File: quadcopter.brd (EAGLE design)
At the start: 130.1 x 130.1 mm, 76 parts, among them J1 AVR_SPI_PRG_6NS, J3 HEADER-0.1IN-2POS-FEMALE, J4 HEADER-0.1IN-2POS-FEMALE, J5 HEADER-0.1IN-2POS-FEMALE, J6 HEADER-0.1IN-2POS-FEMALE, SW1 PUSHBUTTON_SMD-VERTICAL, SW2 PUSHBUTTON_SMD-VERTICAL, U1 ATMEGA128RFA1

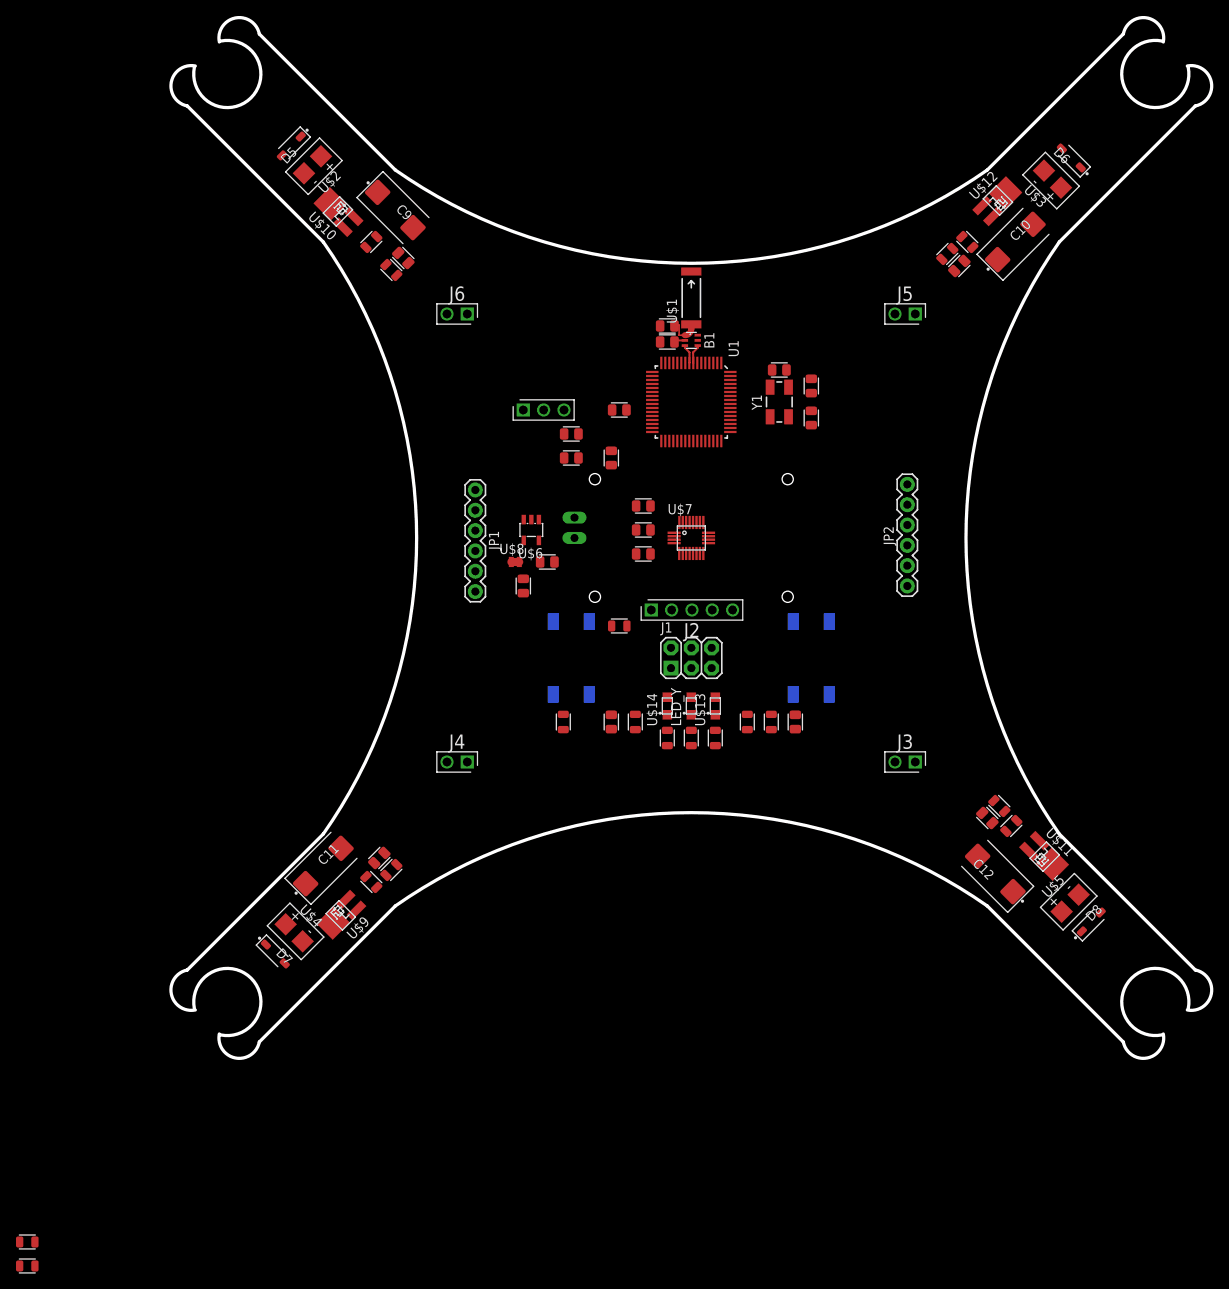
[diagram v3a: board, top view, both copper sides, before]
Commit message: layed down bat plane
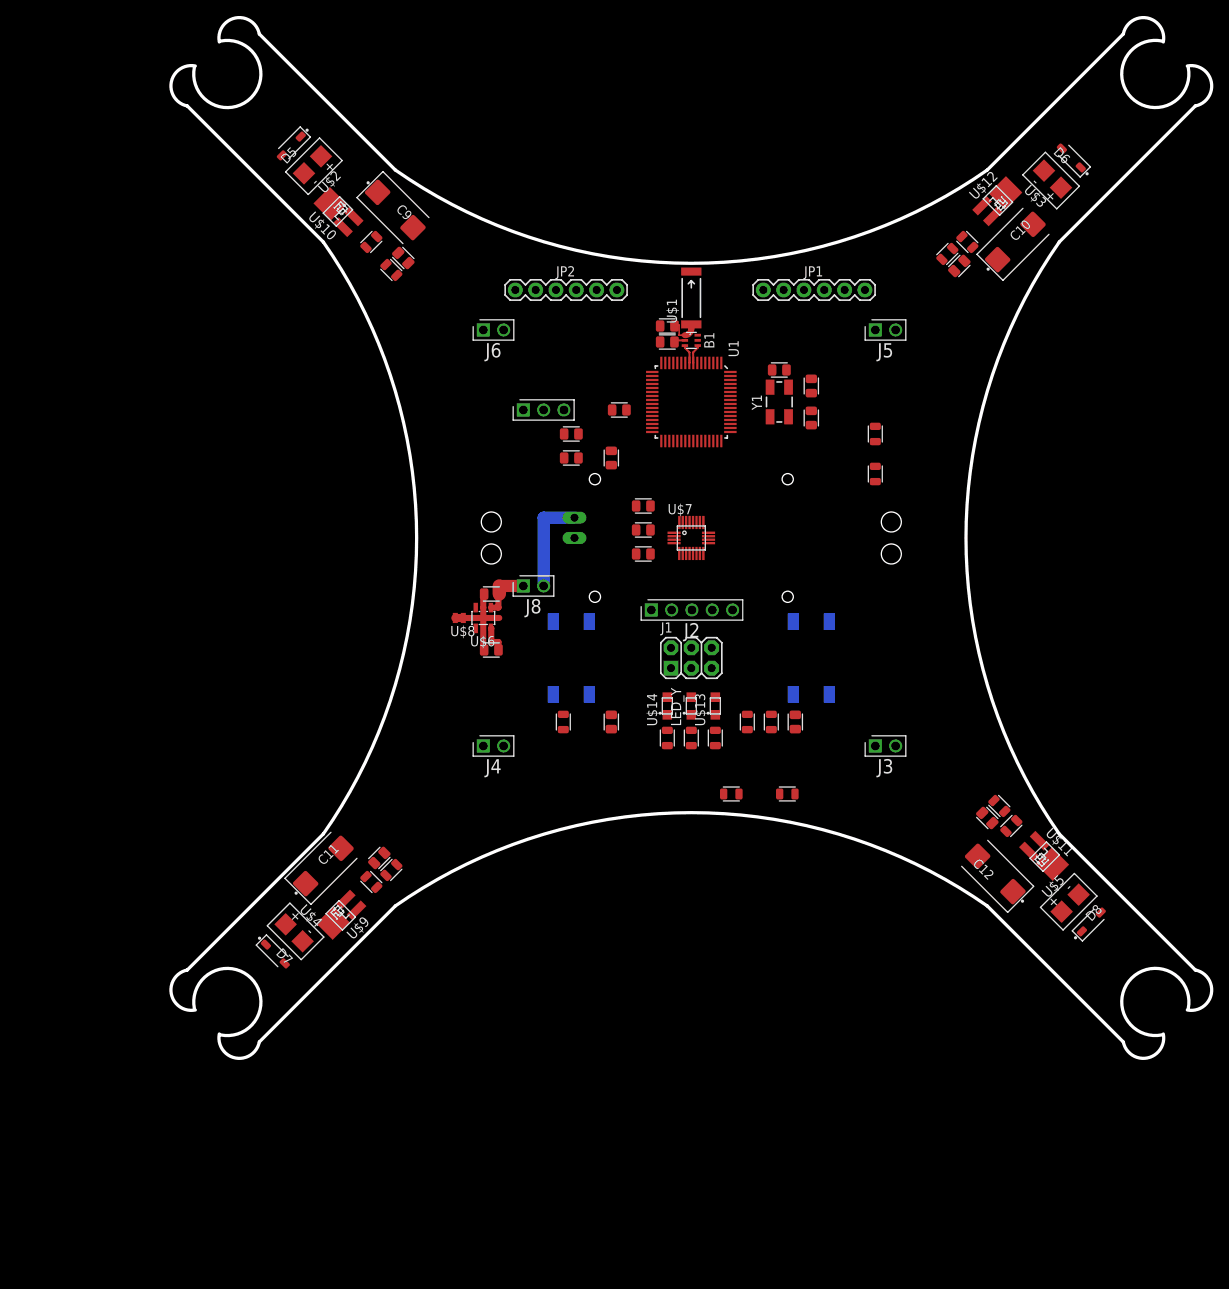
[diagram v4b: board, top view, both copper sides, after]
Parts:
- added J8: HEADER-0.1IN-2POS-FEMALE, Components:HDRV2W63P254_2X1_508X254H838_HS
- moved R14 110.3 mm to (12.0, -32.0)
- moved R18 105.9 mm to (5.00, -32.0), turned to 180 degrees
- moved JP2 61.4 mm to (-22.0, 31.0), turned to 0 degrees
- moved JP1 43.8 mm to (9.00, 31.0), turned to 0 degrees
- moved R13 43.1 mm to (23.0, 8.00)
- moved R12 40.0 mm to (23.0, 13.0), turned to 270 degrees
- moved C17 13.0 mm to (-25.0, -14.0), turned to 0 degrees
- moved U$6 12.5 mm to (-26.0, -10.0)
- moved U$8 9.90 mm to (-29.0, -10.0), turned to 180 degrees
- moved J3 5.39 mm to (23.0, -26.0), turned to 0 degrees
- moved J5 5.39 mm to (23.0, 26.0), turned to 0 degrees
- moved C16 4.12 mm to (-25.0, -7.00), turned to 180 degrees
- moved J4 2.83 mm to (-26.0, -26.0), turned to 0 degrees
- moved J6 2.83 mm to (-26.0, 26.0), turned to 0 degrees
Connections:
- new net N$10: BATT1.+, J8.2
- net V_BAT: now also J8.1; no longer BATT1.+
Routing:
- net V_BAT: track 0.00 -> 19.6 mm
- net N$10: track 0.00 -> 12.4 mm
- net GND: track 0.00 -> 11.6 mm
- net VCC: track 0.00 -> 3.64 mm
- added copper zone on layer 2, net V_BAT

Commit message: Layed out power planes
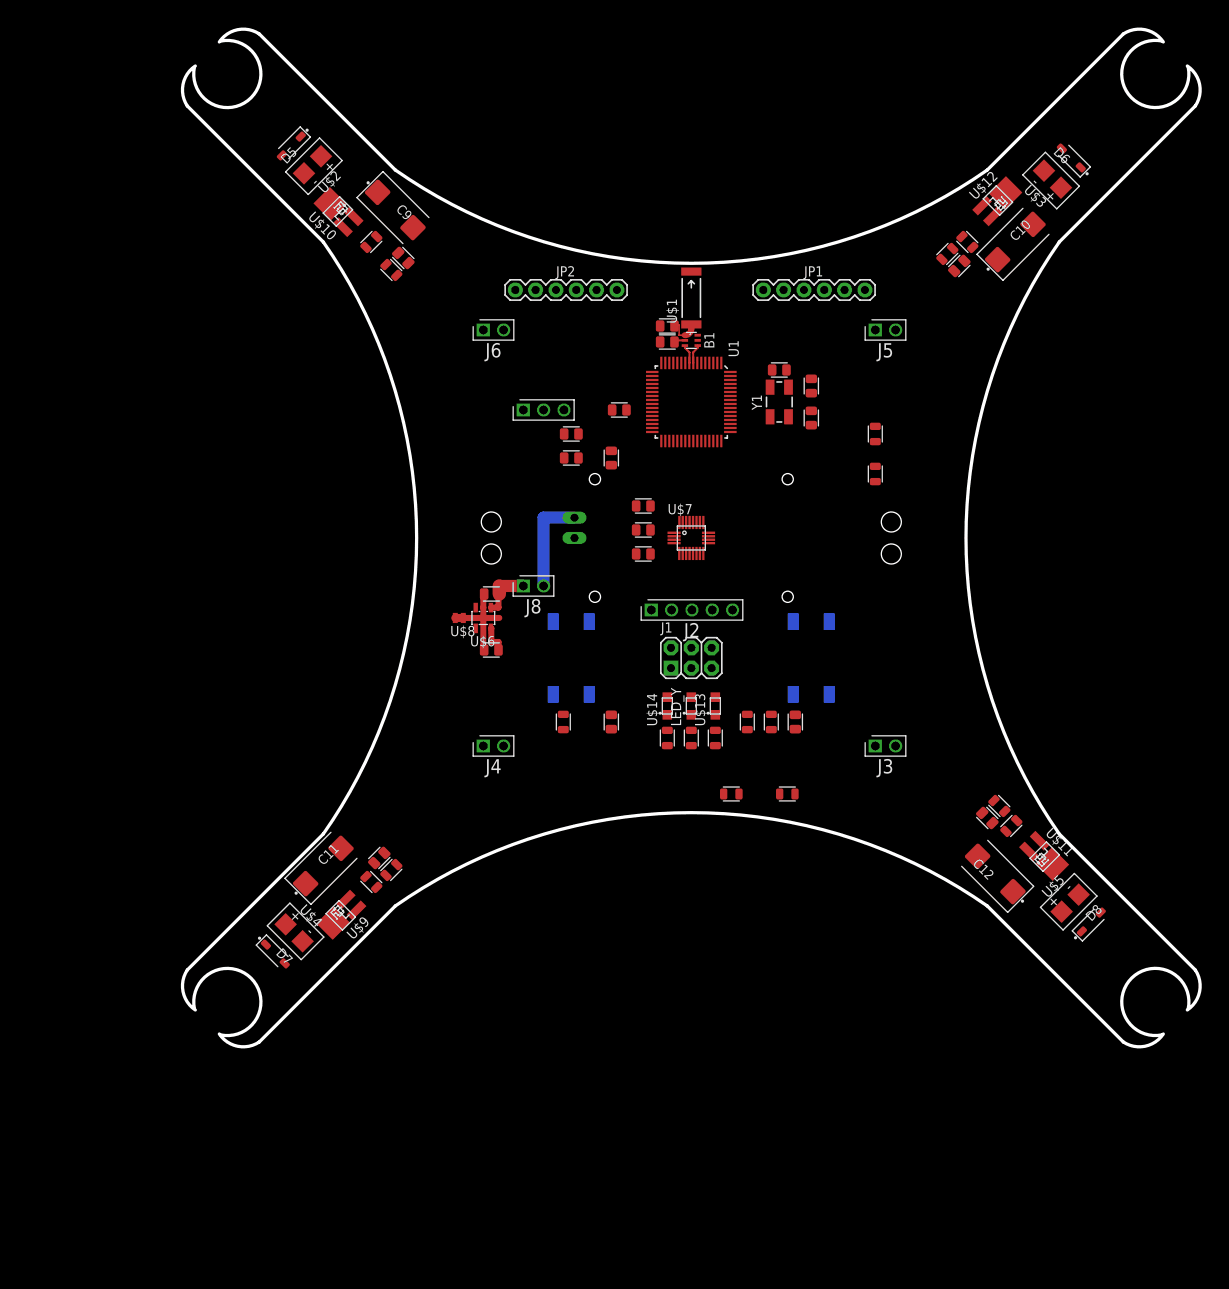
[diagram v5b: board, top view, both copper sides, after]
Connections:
- net MOTOR_GND renamed BAT_GND
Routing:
- added copper zone on layer 15, net BAT_GND
- added copper zone on layer 15, net GND
- added copper zone on layer 2, net VCC
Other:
- board size 130.1 x 130.1 mm -> 127.2 x 127.2 mm

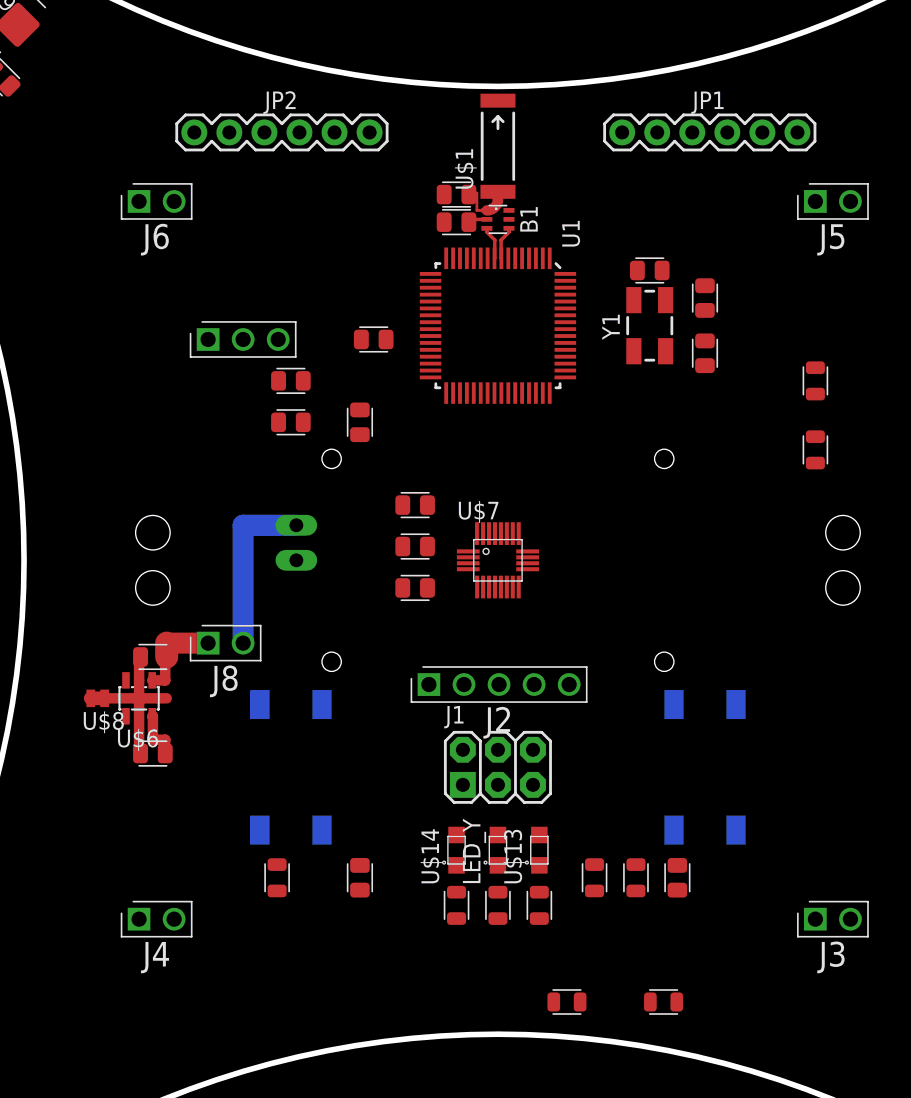
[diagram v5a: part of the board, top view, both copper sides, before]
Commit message: found a much better way to layout pours
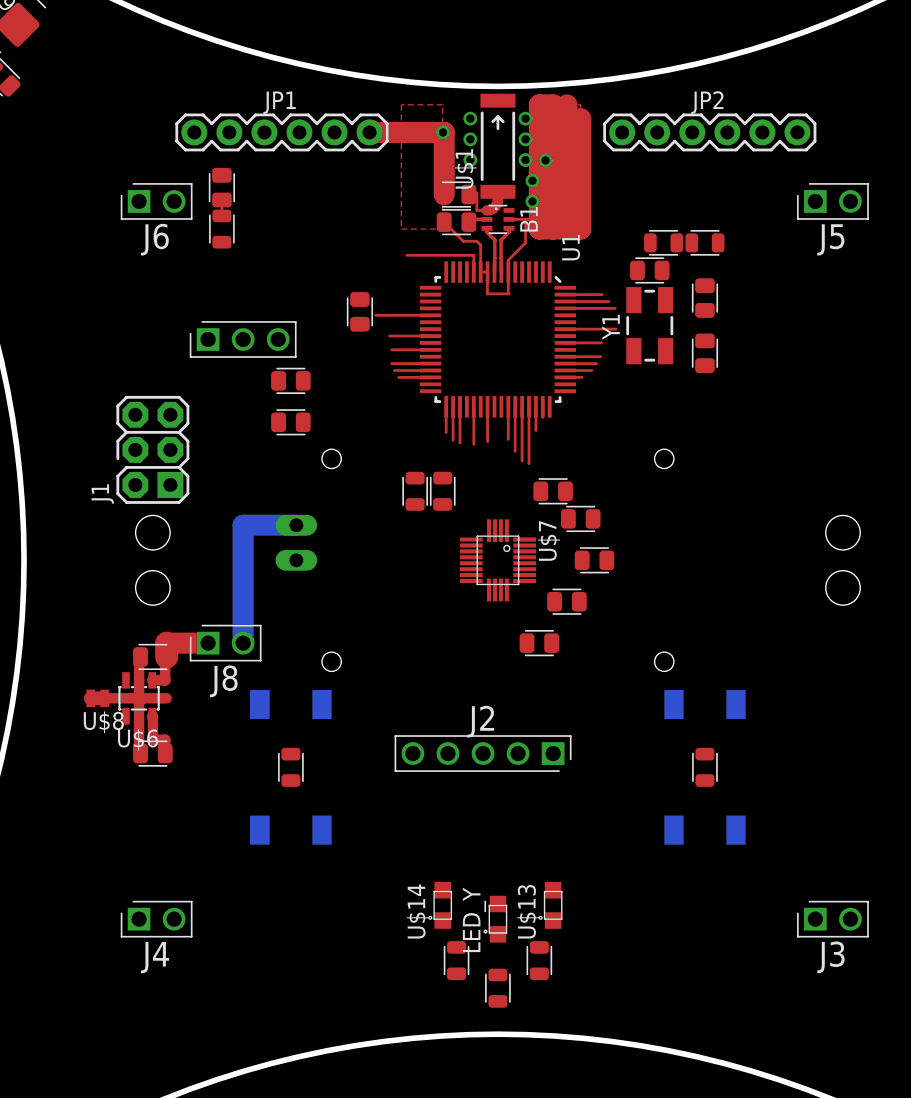
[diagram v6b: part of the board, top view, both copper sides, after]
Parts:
- moved R3 55.8 mm to (-20.0, 24.0), turned to 270 degrees
- moved R14 40.3 mm to (-4.00, 5.00), turned to 270 degrees
- moved R18 38.6 mm to (-6.00, 5.00), turned to 270 degrees
- moved J1 34.0 mm to (-25.0, 8.00), turned to 90 degrees
- moved JP1 31.0 mm to (-22.0, 31.0)
- moved JP2 31.0 mm to (9.00, 31.0)
- moved C8 30.5 mm to (6.00, 3.00), turned to 0 degrees
- moved C6 23.8 mm to (7.00, 0.00), turned to 0 degrees
- moved C5 19.7 mm to (-20.0, 27.0), turned to 90 degrees
- moved R13 17.0 mm to (15.0, 23.0), turned to 180 degrees
- moved R12 14.9 mm to (12.0, 23.0), turned to 180 degrees
- moved C13 11.4 mm to (3.00, -6.00), turned to 180 degrees
- moved R16 11.3 mm to (15.0, -15.0)
- moved C14 11.0 mm to (5.00, -3.00), turned to 0 degrees
- moved J2 10.3 mm to (4.00, -14.0), turned to 180 degrees
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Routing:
- net GND: track 11.6 -> 90.7 mm, vias 0 -> 2
- net N$22: track 0.00 -> 30.0 mm
- net VCC: track 3.64 -> 15.7 mm
- net N$23: track 0.00 -> 8.00 mm
- net RESET: track 0.00 -> 7.20 mm
- net N$20: track 0.00 -> 3.97 mm
- net N$2: track 0.00 -> 3.22 mm
- net TX1: track 0.00 -> 2.82 mm
- net SDA: track 0.00 -> 2.82 mm
- net SCK: track 0.00 -> 2.72 mm
- net BAT_SENSE: track 0.00 -> 2.67 mm
- net N$19: track 0.00 -> 2.62 mm
- net M3_CTL: track 0.00 -> 2.62 mm
- net MISO: track 0.00 -> 2.52 mm
- net N$4: track 0.00 -> 2.37 mm
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- added copper zone on layer 1, net GND
- added copper zone on layer 2, net GND
- added copper zone on layer 1, net N$16

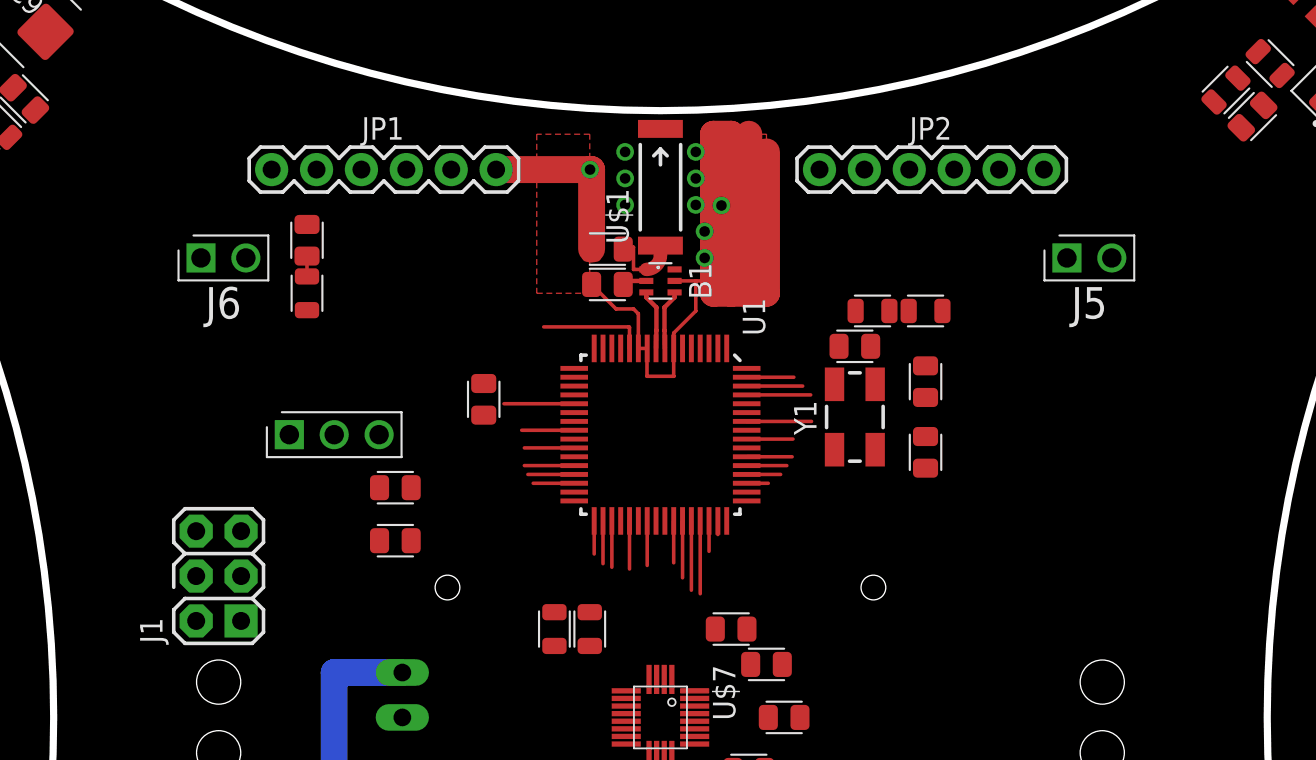
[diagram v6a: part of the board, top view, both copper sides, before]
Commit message: further isolated attenna
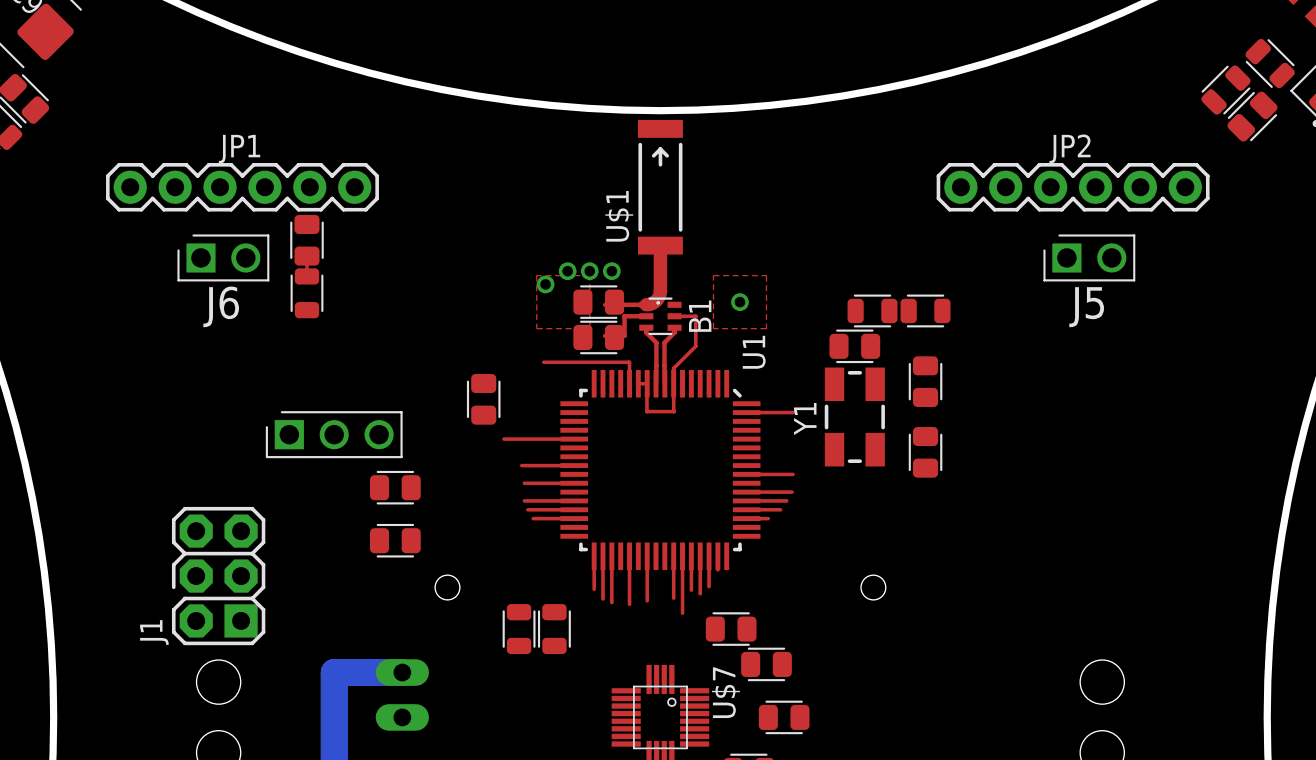
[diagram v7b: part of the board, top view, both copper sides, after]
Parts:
- moved JP1 8.06 mm to (-30.0, 30.0)
- moved JP2 8.06 mm to (17.0, 30.0)
- moved C1 3.04 mm to (-3.49, 21.5)
- moved C2 3.04 mm to (-3.49, 23.5)
- moved B1 2.00 mm to (0.00, 22.7)
- moved R14 2.00 mm to (-6.00, 5.00)
- moved R18 2.00 mm to (-8.00, 5.00)
- moved U1 2.00 mm to (0.00, 14.0)
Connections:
- net BAT_GND: now also C9.2
- net GND: no longer C9.2
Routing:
- net GND: track 90.7 -> 31.9 mm, vias 2 -> 0
- net N$22: track 30.0 -> 0.00 mm, vias 0 -> 1
- net N$23: track 8.00 -> 0.00 mm, vias 0 -> 1
- net VCC: track 15.7 -> 10.6 mm
- net N$3: track 1.50 -> 3.93 mm
- net ATTENNA: track 4.35 -> 6.51 mm

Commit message: preautoroute
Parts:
- moved R17 8.00 mm to (0.00, -23.0)
- moved LED_Y 7.00 mm to (0.00, -19.0)
- moved R1 5.00 mm to (3.00, -24.0)
- moved R2 5.00 mm to (-3.00, -24.0)
- moved U$13 5.00 mm to (4.00, -20.0)
- moved U$14 5.00 mm to (-4.00, -20.0)
